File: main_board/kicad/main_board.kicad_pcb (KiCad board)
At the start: 2 copper layers, 1 part, among them U1 Teensy4.1

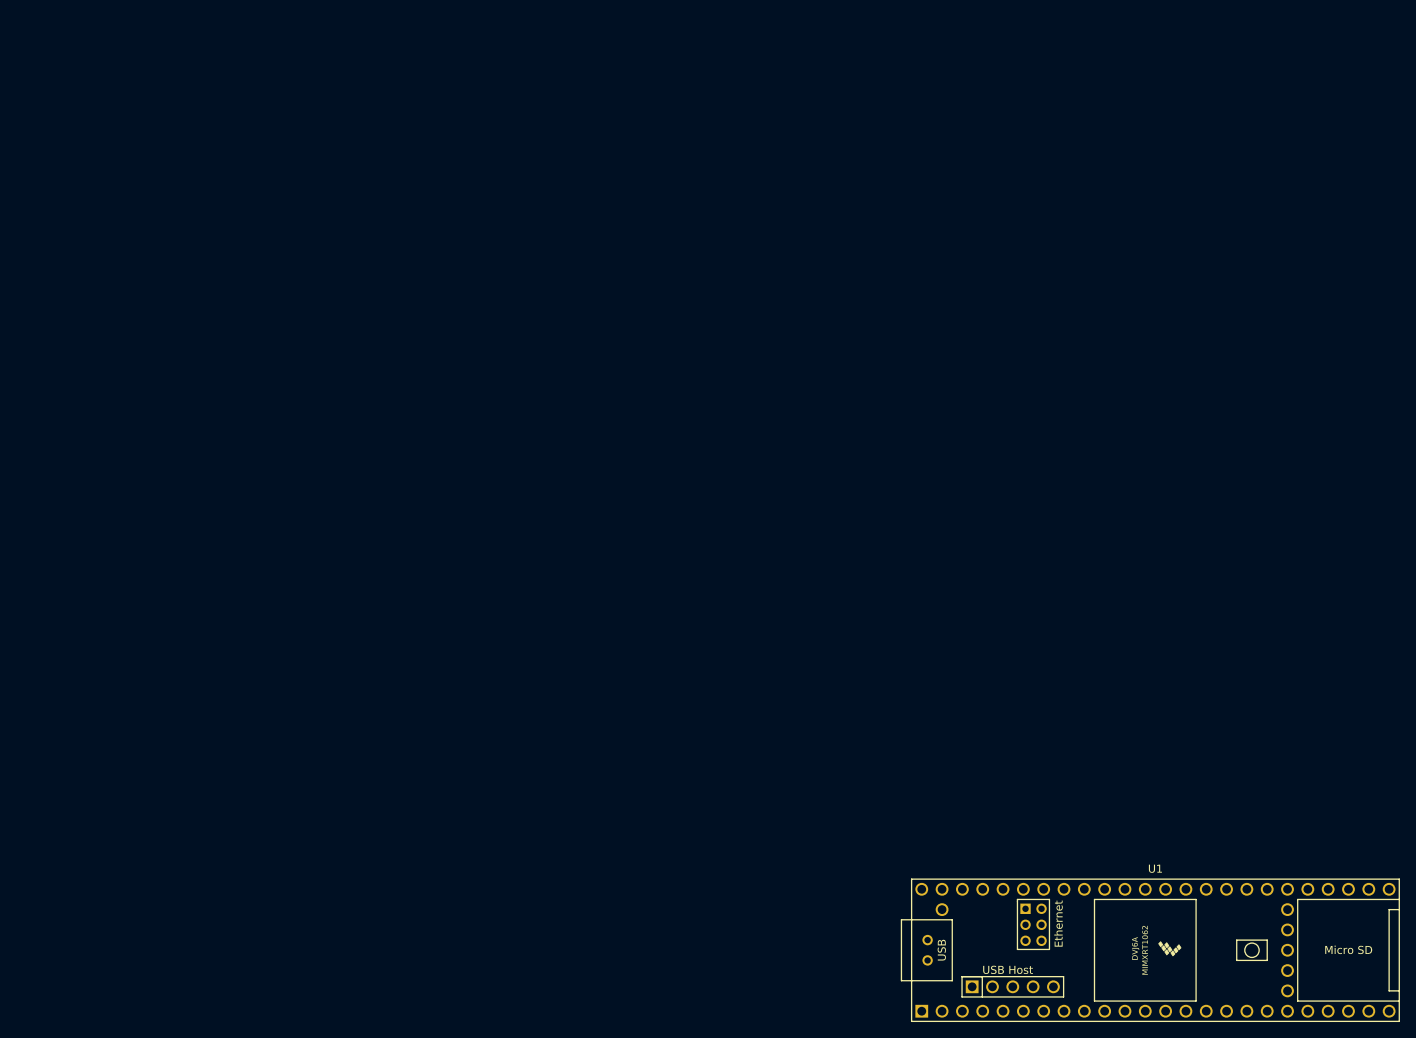
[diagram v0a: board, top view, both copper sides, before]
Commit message: Added pcie edge footprint.
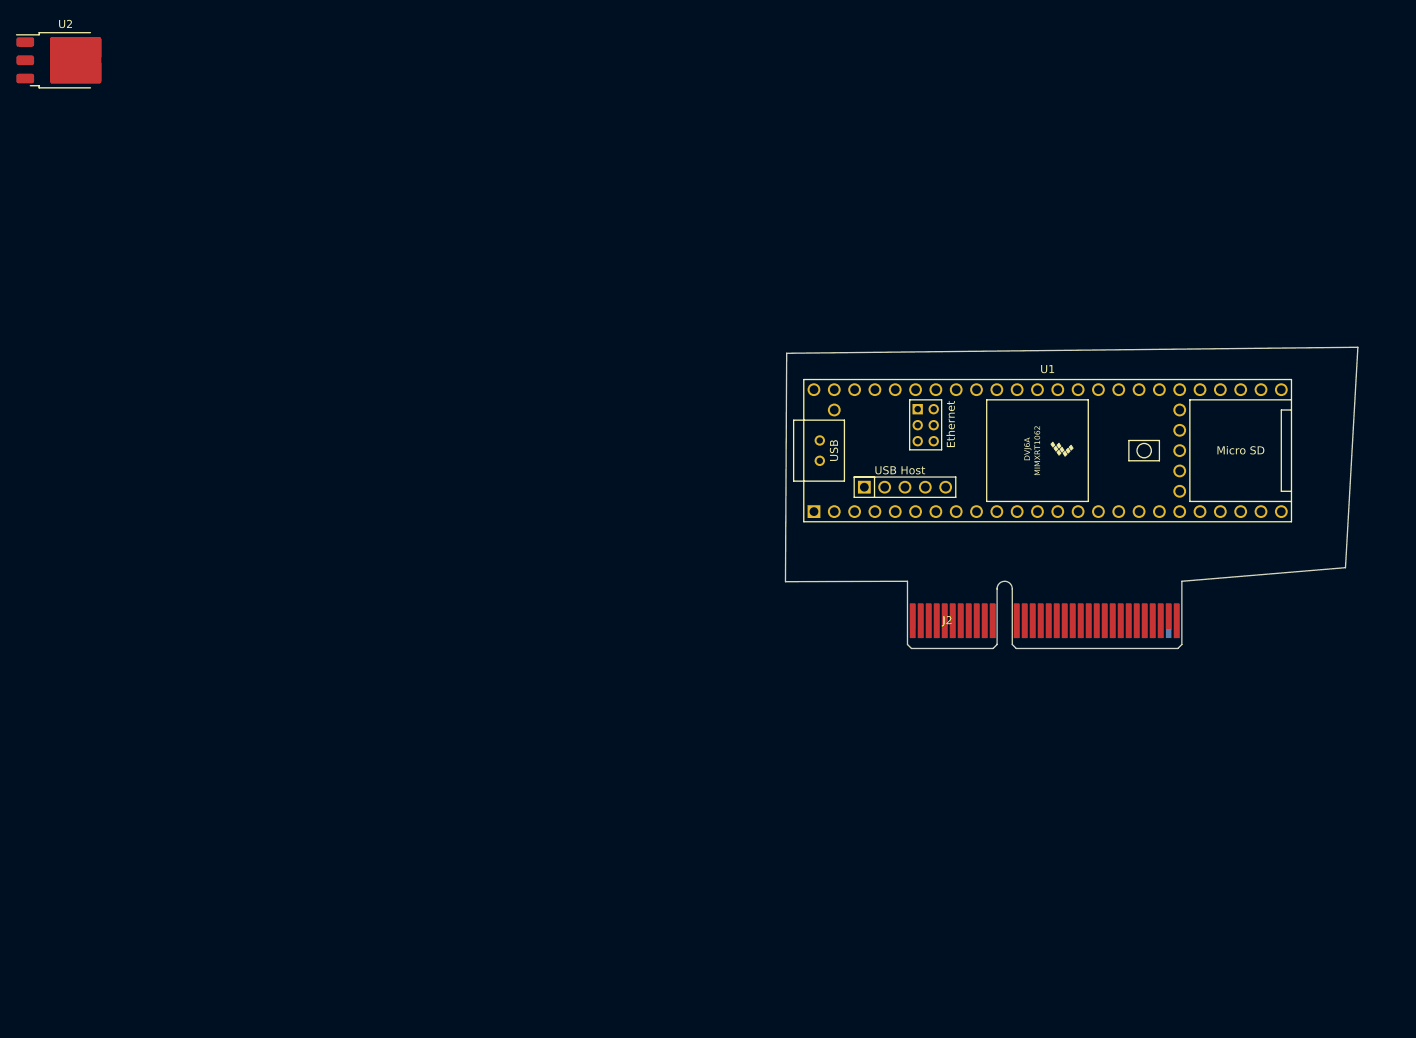
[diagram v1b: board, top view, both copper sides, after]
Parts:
- added J2: PCIE_64, main_board:pcie_64, F.Cu at (111.7, 87.5)
- added U2: 5V, Package_TO_SOT_SMD:TO-252-3_TabPin2, F.Cu at (6.42, 14.0)
- moved U1 63.9 mm to (129.2, 62.8)
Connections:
- U1 pad 48: unconnected-(U1-VIN-Pad48) -> /VIN
- U1 pad 49: unconnected-(U1-VUSB-Pad49) -> /VUSB
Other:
- board outline added: 71.5 x 29.3 mm

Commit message: Progress with main board footprints.
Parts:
- removed U1: Teensy4.1, main_board:Teensy41
- removed U2: 5V, Package_TO_SOT_SMD:TO-252-3_TabPin2
- added J1: pcie_98, main_board:pcie_98_socket, F.Cu at (93.9, 37.0)
- added J3: pcie_98, main_board:pcie_98_socket, F.Cu at (109.4, 36.8)
- added J4: pcie_98, main_board:pcie_98_socket, F.Cu at (123.9, 36.9)
- added J5: pcie_98, main_board:pcie_98_socket, F.Cu at (138.3, 36.9)
- added RN1: R_Pack06, main_board:weact_stm32fh750, F.Cu at (39.6, 62.0)
- J2: value PCIE_64 -> pcie_98; footprint main_board:pcie_64 -> main_board:pcie_98_socket
- moved J2 59.8 mm to (79.4, 37.1), turned to -90 degrees
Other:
- board size 71.5 x 29.3 mm -> 132.3 x 80.9 mm
